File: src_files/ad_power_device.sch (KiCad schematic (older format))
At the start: 24 parts, among them J2 5622-6309-ML, J3 205957-0271, J7 Conn_01x05_Male, U11 NFC_VS1797SM

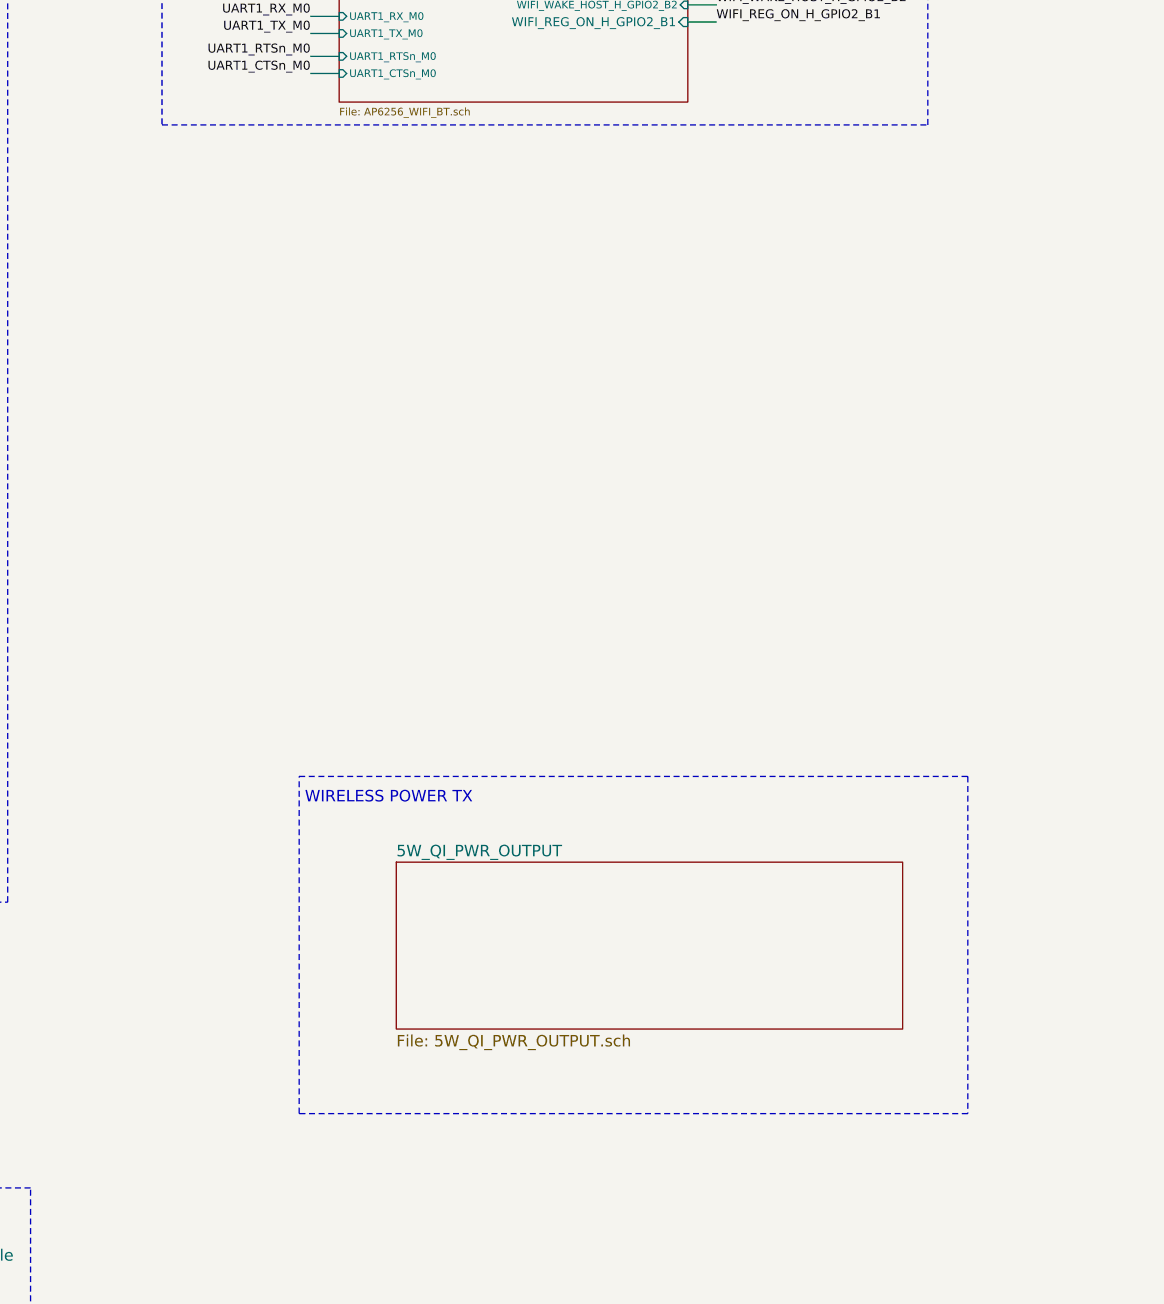
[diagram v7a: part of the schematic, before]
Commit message: added usb power output
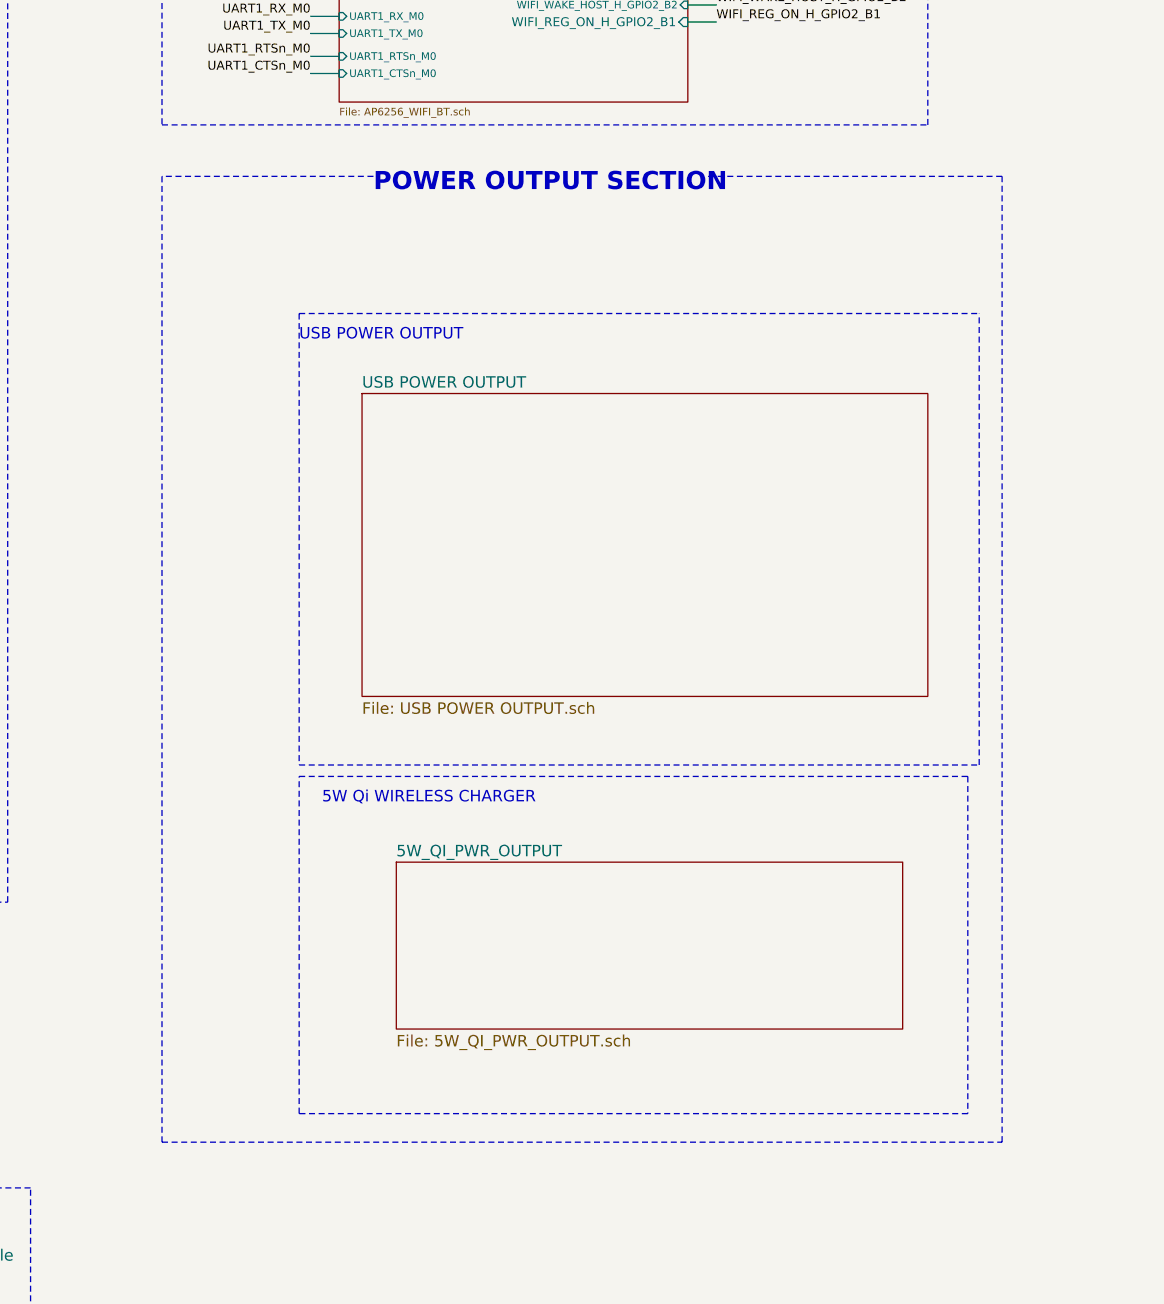
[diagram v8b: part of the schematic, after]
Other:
- note added: "5W Qi WIRELESS CHARGER"
- note added: "POWER OUTPUT SECTION"
- note added: "USB POWER OUTPUT"
- note removed: "WIRELESS POWER TX"
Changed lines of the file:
@@
 $Descr A3 16535 11693
 encoding utf-8
-Sheet 1 16
+Sheet 1 17
 Title ""
 Date ""
@@
 Wire Notes Line
 	12900 8300 15825 8300
-Text Notes 12925 8425 0    50   ~ 0
-WIRELESS POWER TX
+$Sheet
+S 13175 6625 2475 1325
+U 639A9535
+F0 "USB POWER OUTPUT" 50
+F1 "USB POWER OUTPUT.sch" 50
+$EndSheet
+Text Notes 13000 8425 0    50   ~ 0
+5W Qi WIRELESS CHARGER
+Text Notes 12900 6400 0    50   ~ 0
+USB POWER OUTPUT
+Wire Notes Line
+	12900 6275 12900 8250
+Wire Notes Line
+	12900 8250 15875 8250
+Wire Notes Line
+	15875 8250 15875 6275
+Wire Notes Line
+	12900 6275 15875 6275
+Text Notes 13225 5750 0    79   ~ 16
+POWER OUTPUT SECTION
+Wire Notes Line
+	13225 5675 12300 5675
+Wire Notes Line
+	12300 5675 12300 9900
+Wire Notes Line
+	12300 9900 15975 9900
+Wire Notes Line
+	15975 9900 15975 5675
+Wire Notes Line
+	15975 5675 14675 5675
 $EndSCHEMATC
